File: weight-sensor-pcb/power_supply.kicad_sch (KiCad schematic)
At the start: 0 parts

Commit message: message
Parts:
- added C1, Cboot, Cin: C_Small, symbol Device:C_Small
- added L1: L, symbol Device:L
- added R1, R2: R_Small, symbol Device:R_Small
- added U1: TPS54202DDC, Package_TO_SOT_SMD:SOT-23-6, symbol Regulator_Switching:TPS54202DDC
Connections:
- new net: R1.2, R2.1, U1.4 (FB)
- new net: Cboot.2, L1.1, U1.2 (SW)
- new net: Cboot.1, U1.6 (BOOT)
- new net +24V: Cin.1, U1.3 (VIN)
- new net GND: C1.2, Cin.2, R2.2, U1.1 (GND)
- new net Vout: C1.1, L1.2, R1.1

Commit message: finish converter schematic
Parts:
- added C2: 56p, symbol Device:C_Small
- added C3: 0.1u, symbol Device:C_Small
- C1: value C_Small -> 44u
- Cboot: value C_Small -> 100nF
- Cin: value C_Small -> 20u
- L1: value L -> 10uH
- R1: value R_Small -> 100k
- R2: value R_Small -> 22.1k
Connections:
- net +24V: now also C3.1
- net GND: now also C3.2
- net Vout: now also C2.1
- net at R1.2, R2.1, U1.4 (FB): now also C2.2
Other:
- note added: ""EN" input is used to turn the converter on and off. According to the datasheet leaving it floating will have it always be on. If this isn't what we want then it could be connected to a microcontroller."
- moved on the sheet: C1, Cin, L1, R1, R2

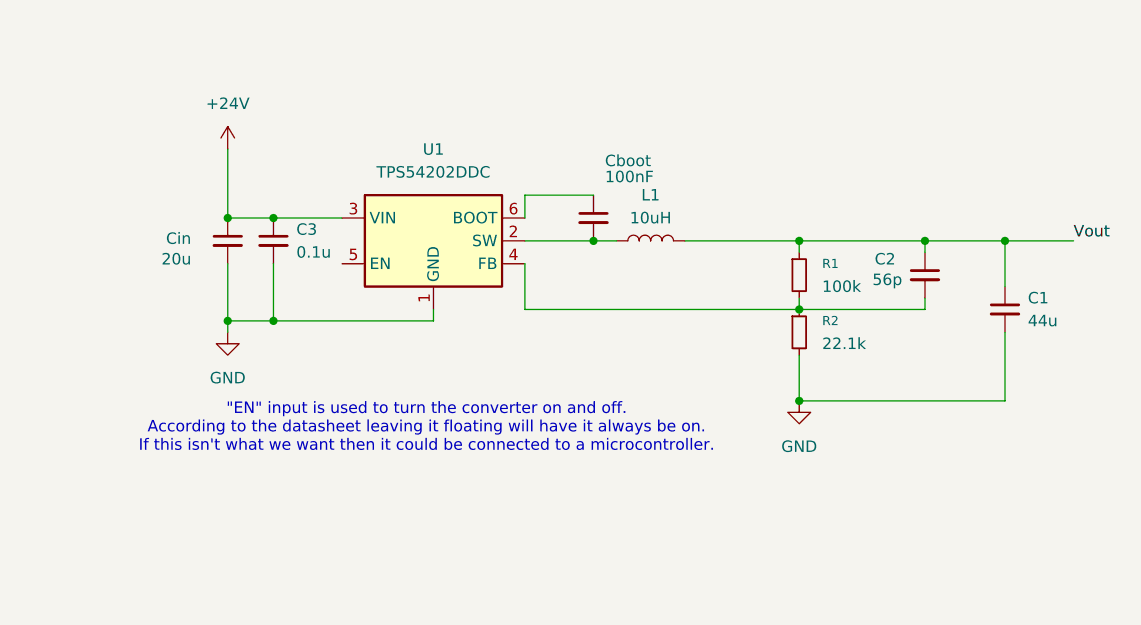
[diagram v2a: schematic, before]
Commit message: Add backup USB power
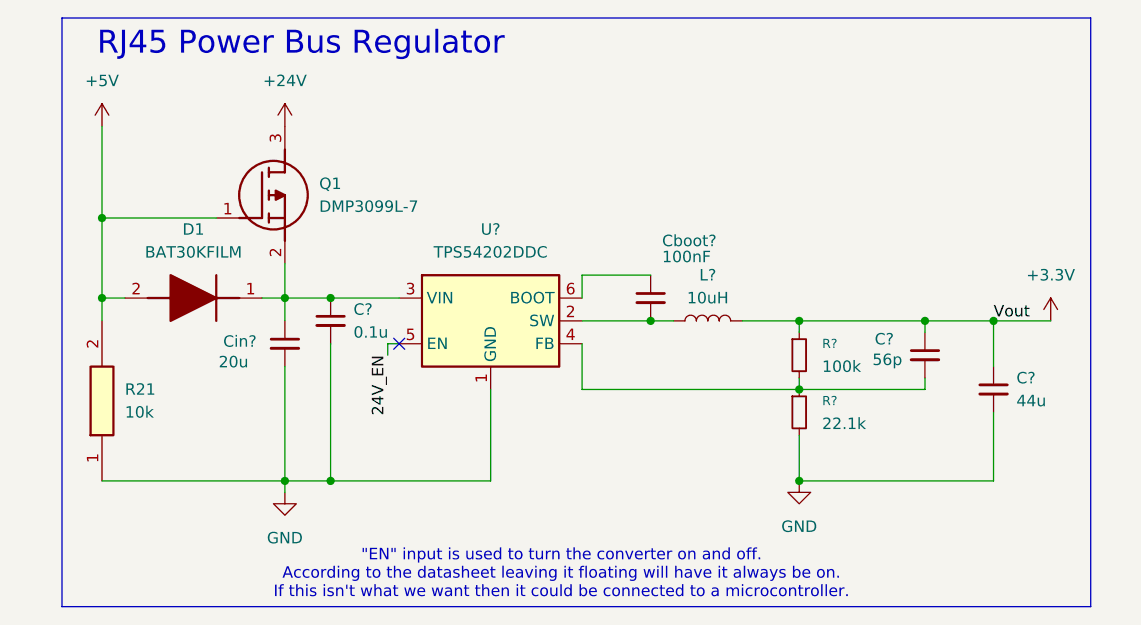
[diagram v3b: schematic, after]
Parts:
- added D1: BAT30KFILM, SODFL1608X70N, symbol Capstone:BAT30KFILM
- added Q1: DMP3099L-7, SOT96P240X115-3N, symbol Capstone:DMP3099L-7
- added R21: 10k, RESC1608X55N, symbol Capstone:RMCF0603FT10K0
- renumbered C3 to C?, C1 to C?, C2 to C?, Cboot to Cboot?, Cin to Cin?, L1 to L?, R2 to R?, R1 to R?, U1 to U?
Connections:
- net +24V: now also Q1.3 (D); no longer C?.1, Cin?.1, U?.3 (VIN)
- net GND: now also R21.1
- net 24V_EN: now reaches U?.5 (EN)
- net Vout renamed +3.3V
- new net: C?.1, Cin?.1, D1.1 (K), Q1.2 (S), U?.3 (VIN)
- new net +5V: D1.2 (A), Q1.1 (G), R21.2
- no-connect marks 0 -> 1
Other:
- note added: "RJ45 Power Bus Regulator"
- moved on the sheet: C?, Cboot?, Cin?, L?, R?, U?

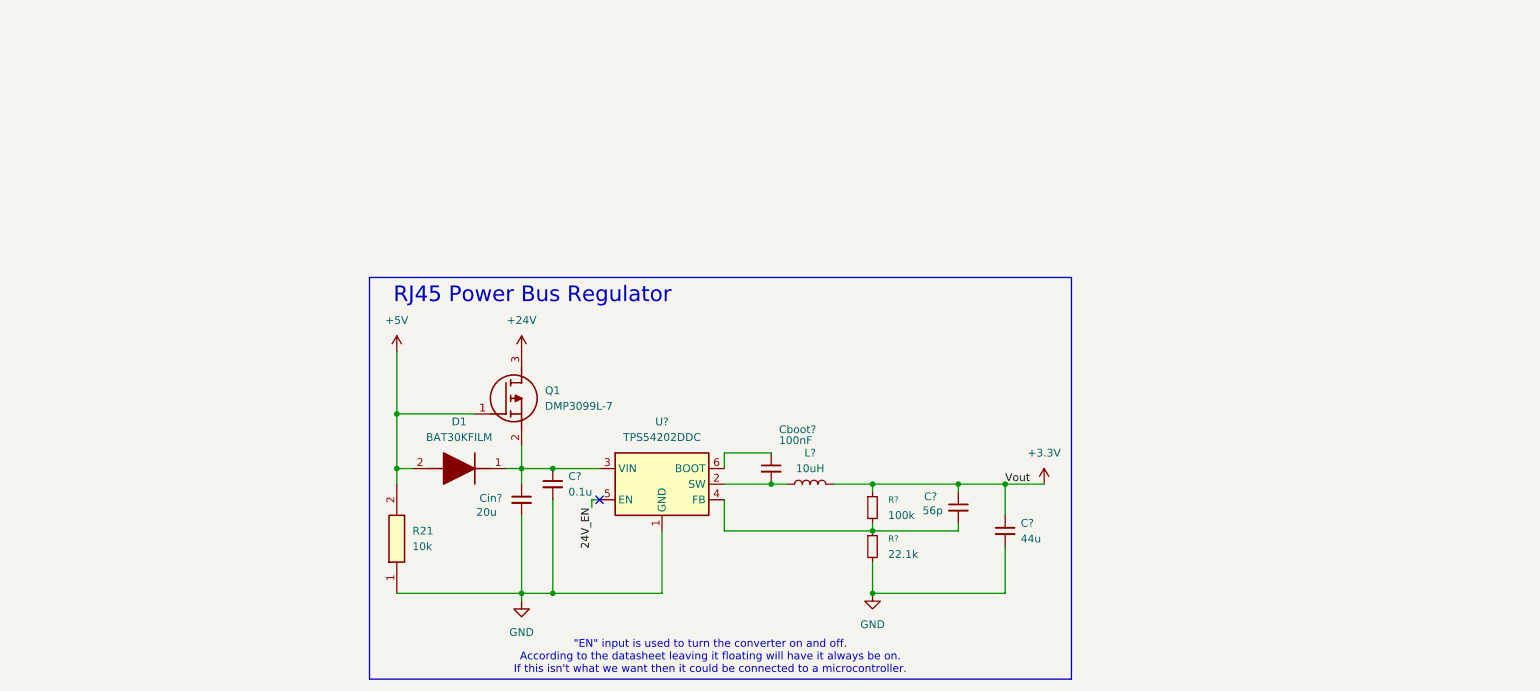
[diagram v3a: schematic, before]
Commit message: Add new buck regulator (no component values)
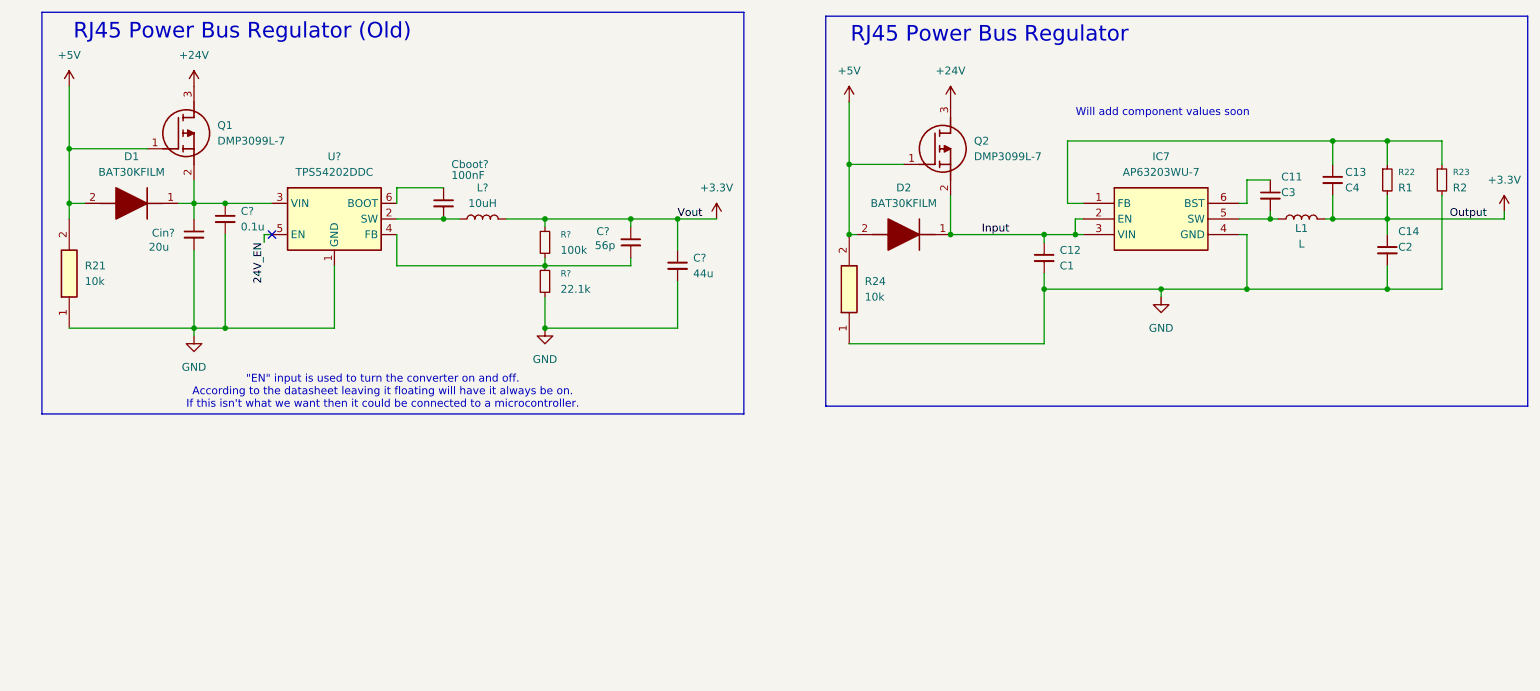
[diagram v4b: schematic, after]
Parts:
- added C11: C3, symbol Device:C_Small
- added C12: C1, symbol Device:C_Small
- added C13: C4, symbol Device:C_Small
- added C14: C2, symbol Device:C_Small
- added D2: BAT30KFILM, SODFL1608X70N, symbol Capstone:BAT30KFILM
- added IC7: AP63203WU-7, AP63203WU7, symbol Capstone:AP63203WU-7
- added L1: L, symbol Device:L
- added Q2: DMP3099L-7, SOT96P240X115-3N, symbol Capstone:DMP3099L-7
- added R22: R1, symbol Device:R_Small
- added R23: R2, symbol Device:R_Small
- added R24: 10k, RESC1608X55N, symbol Capstone:RMCF0603FT10K0
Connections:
- net +24V: now also Q2.3 (D)
- net +3.3V: now also C13.2, C14.1, L1.2, R22.2
- net +5V: now also D2.2 (A), Q2.1 (G), R24.2
- net GND: now also C12.2, C14.2, IC7.4 (GND), R23.2, R24.1
- new net: C11.2, IC7.5 (SW), L1.1
- new net: C13.1, IC7.1 (FB), R22.1, R23.1
- new net: C11.1, IC7.6 (BST)
- new net Input: C12.1, D2.1 (K), IC7.2 (EN), IC7.3 (VIN), Q2.2 (S)
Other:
- note added: "RJ45 Power Bus Regulator (Old)"
- note added: "Will add component values soon"
- moved on the sheet: C?, Cboot?, Cin?, D1, L?, Q1, R21, R?, U?

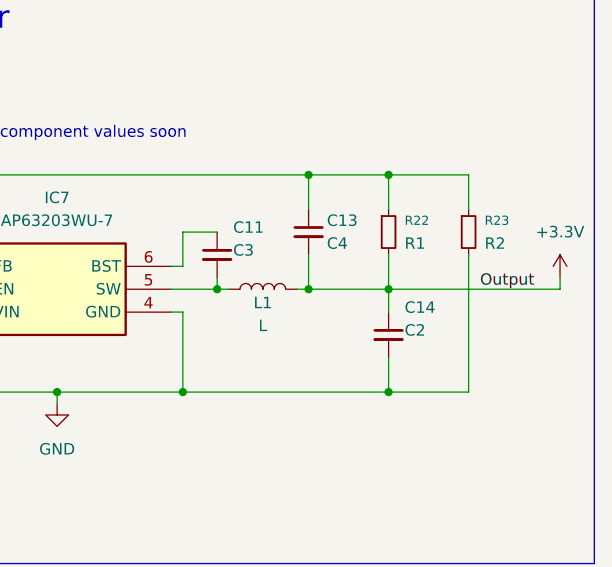
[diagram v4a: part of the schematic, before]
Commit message: update new buck regulator schematic
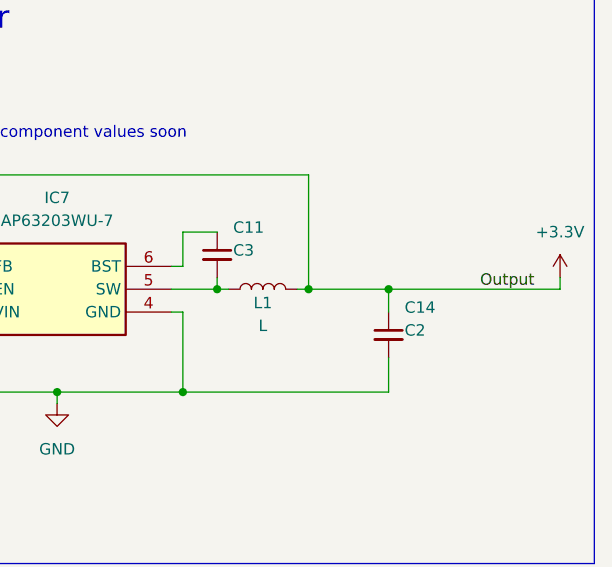
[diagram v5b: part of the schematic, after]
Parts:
- removed C13: C4, symbol Device:C_Small
- removed R22: R1, symbol Device:R_Small
- removed R23: R2, symbol Device:R_Small
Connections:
- net +3.3V: now also IC7.1 (FB)

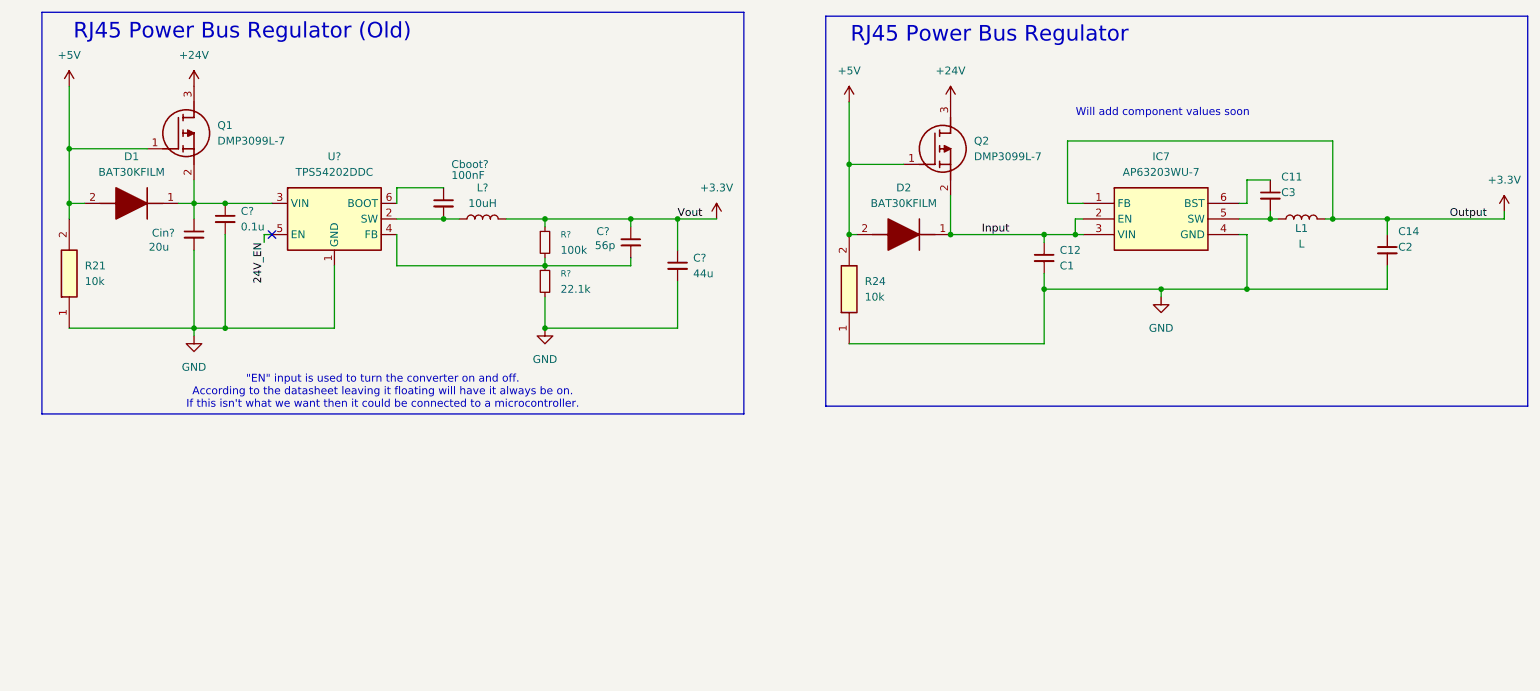
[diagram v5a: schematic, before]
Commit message: Add parts to use in 3.3v buck regulator
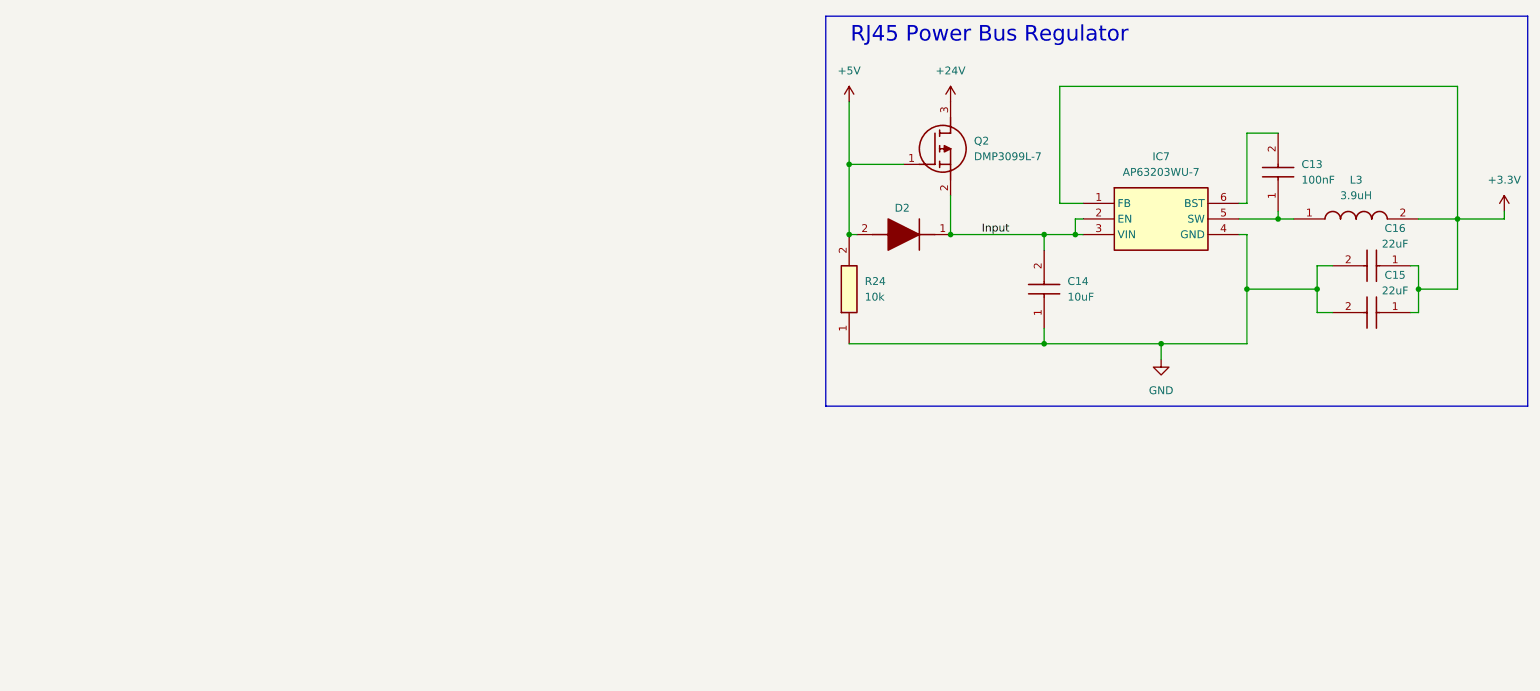
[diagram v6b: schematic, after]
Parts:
- removed C11: C3, symbol Device:C_Small
- removed C12: C1, symbol Device:C_Small
- removed C14: C2, symbol Device:C_Small
- removed C?: 0.1u, symbol Device:C_Small
- removed C?: 44u, symbol Device:C_Small
- removed C?: 56p, symbol Device:C_Small
- removed Cboot?: 100nF, symbol Device:C_Small
- removed Cin?: 20u, symbol Device:C_Small
- removed D1: BAT30KFILM, SODFL1608X70N, symbol Capstone:BAT30KFILM
- removed L1: L, symbol Device:L
- removed L?: 10uH, symbol Device:L
- removed Q1: DMP3099L-7, SOT96P240X115-3N, symbol Capstone:DMP3099L-7
- removed R21: 10k, RESC1608X55N, symbol Capstone:RMCF0603FT10K0
- removed R?: 22.1k, symbol Device:R_Small
- removed R?: 100k, symbol Device:R_Small
- removed U?: TPS54202DDC, Package_TO_SOT_SMD:SOT-23-6, symbol Regulator_Switching:TPS54202DDC
- added C13: 100nF, CAPC1005X70N, symbol Capstone:GRM155R70J104KA01D
- added C14: 10uF, CAPC2012X145N, symbol Capstone:GRM21BR61E106KA73K
- added C15, C16: 22uF, CAPC3216X190N, symbol Capstone:TMK316BBJ226ML-T
- added L3: 3.9uH, ASPI0628150MT1, symbol Capstone:ASPI-0628-3R9M-T1
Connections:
- net +3.3V: now also C15.1, C16.1, L3.2
- net GND: now also C14.1, C15.2, C16.2
- net Input: now also C14.2
- net at IC7.5 (SW): now also C13.1, L3.1
- net at IC7.6 (BST): now also C13.2
- no-connect marks 1 -> 0
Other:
- note removed: ""EN" input is used to turn the converter on and off. According to the datasheet leaving it floating will have it always be on. If this isn't what we want then it could be connected to a microcontroller."
- note removed: "RJ45 Power Bus Regulator (Old)"
- note removed: "Will add component values soon"

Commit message: layout progress 1
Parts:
- added IC6: LM2776DBVR, SOT95P280X145-6N, symbol Capstone:LM2776DBVR
- added TP21: SW, TestPoint:TestPoint_Pad_D1.5mm, symbol Connector:TestPoint
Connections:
- net GND: now also IC6.2 (GND)
- net SW: now reaches C13.1, IC7.5 (SW), L3.1
- net SW: now also TP21.1
- net Input renamed VIN
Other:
- note added: "Test Points"

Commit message: Layout draft complete
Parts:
- added C10, C11: 2.2uF, CAPC1608X90N, symbol Capstone:GRM1885C1H222JA01D
- added C12: 1uF, CAPC1005X70N, symbol Capstone:GRM155R70J105KA12D
- renumbered C14 to C13, C13 to C14, C16 to C15, C15 to C16, D2 to D1, IC6 to IC5, IC7 to IC6, L3 to L1, Q2 to Q1, R24 to R22, TP21 to TP16
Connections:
- net +3.3V: now also IC5.3 (VIN), IC5.4 (EN), C11.1
- net GND: now also C10.2, C11.2
- net -3V3: now reaches IC5.1 (VOUT)
- net -3V3: now also C10.1
- net at IC5.5 (C1+): now also C12.1
- net at IC5.6 (C1-): now also C12.2
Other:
- note added: "Voltage Inverter"
- moved on the sheet: IC5, TP16
